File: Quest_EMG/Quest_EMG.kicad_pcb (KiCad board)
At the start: 2 copper layers, 55 x 60 mm, 72 parts, among them IC1 OPA2890IDGST, IC2 OPA2890IDGST, J1 Conn_01x19_Socket, J2 Conn_01x19_Socket, J3 AudioJack3, J4 AudioJack3, J5 Conn_01x10_Pin, U1 AD8620, U2 INA121UAE4, U3 INA121UAE4, U4 L7805

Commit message: cleanup
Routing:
- net GND: vias 104 -> 108
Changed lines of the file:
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@@
       (effects (font (size 0.6 0.6) (thickness 0.15) bold) (justify left top mirror))
     (stroke (width 0.15) (type solid))  )
+  (dimension (type aligned) (layer "User.2")
+    (pts (xy 84.57 79.02) (xy 139.57 79.02))
+    (height 4.011)
+    (gr_text "55.0000 mm" (at 112.07 81.881) (layer "User.2")
+      (effects (font (size 1 1) (thickness 0.15)))
+    )
+    (format (prefix "") (suffix "") (units 3) (units_format 1) (precision 4))
+    (style (thickness 0.15) (arrow_length 1.27) (text_position_mode 0) (extension_height 0.58642) (extension_offset 0.5) keep_text_aligned)
+  )
+  (dimension (type aligned) (layer "User.2")
+    (pts (xy 84.57 79.02) (xy 84.57 19.02))
+    (height -3.385)
+    (gr_text "60.0000 mm" (at 80.035 49.02 90) (layer "User.2")
+      (effects (font (size 1 1) (thickness 0.15)))
+    )
+    (format (prefix "") (suffix "") (units 3) (units_format 1) (precision 4))
+    (style (thickness 0.15) (arrow_length 1.27) (text_position_mode 0) (extension_height 0.58642) (extension_offset 0.5) keep_text_aligned)
+  )
   (segment (start 96.042501 55.297501) (end 96.042501 57.498501) (width 0.25) (layer "F.Cu") (net 1))
   (segment (start 120.767 69.598) (end 121.649 69.598) (width 0.25) (layer "F.Cu") (net 1))
@@
   (via (at 94.831 73.982) (size 0.8) (drill 0.4) (layers "F.Cu" "B.Cu") (free) (net 1))
   (via (at 133.871 65.097) (size 0.8) (drill 0.4) (layers "F.Cu" "B.Cu") (free) (net 1))
+  (via (at 119.486 39.508) (size 0.8) (drill 0.4) (layers "F.Cu" "B.Cu") (free) (net 1))
   (via (at 90.833 71.341) (size 0.8) (drill 0.4) (layers "F.Cu" "B.Cu") (free) (net 1))
   (via (at 130.735 50.407) (size 0.8) (drill 0.4) (layers "F.Cu" "B.Cu") (free) (net 1))
@@
   (via (at 130.68 64.767) (size 0.8) (drill 0.4) (layers "F.Cu" "B.Cu") (free) (net 1))
   (via (at 108.565 26.591) (size 0.8) (drill 0.4) (layers "F.Cu" "B.Cu") (free) (net 1))
+  (via (at 119.405 37.09) (size 0.8) (drill 0.4) (layers "F.Cu" "B.Cu") (free) (net 1))
   (via (at 88.706 71.635) (size 0.8) (drill 0.4) (layers "F.Cu" "B.Cu") (free) (net 1))
   (via (at 114.287 22.088) (size 0.8) (drill 0.4) (layers "F.Cu" "B.Cu") (free) (net 1))
@@
   (via (at 100.48 69.58) (size 0.8) (drill 0.4) (layers "F.Cu" "B.Cu") (free) (net 1))
   (via (at 100.554 72.001) (size 0.8) (drill 0.4) (layers "F.Cu" "B.Cu") (free) (net 1))
+  (via (at 114.649 36.929) (size 0.8) (drill 0.4) (layers "F.Cu" "B.Cu") (free) (net 1))
   (via (at 127.214 68.618) (size 0.8) (drill 0.4) (layers "F.Cu" "B.Cu") (free) (net 1))
   (via (at 122.943 41.923) (size 0.8) (drill 0.4) (layers "F.Cu" "B.Cu") (free) (net 1))
@@
   (via (at 126.248 36.651) (size 0.8) (drill 0.4) (layers "F.Cu" "B.Cu") (free) (net 1))
   (via (at 130.735 55.138) (size 0.8) (drill 0.4) (layers "F.Cu" "B.Cu") (free) (net 1))
+  (via (at 126.337 39.428) (size 0.8) (drill 0.4) (layers "F.Cu" "B.Cu") (free) (net 1))
   (via (at 121.697 30.01) (size 0.8) (drill 0.4) (layers "F.Cu" "B.Cu") (free) (net 1))
   (via (at 93.071 71.671) (size 0.8) (drill 0.4) (layers "F.Cu" "B.Cu") (free) (net 1))
@@
       )
     )
-  )
-  (zone (net 0) (net_name "") (layer "B.Cu") (hatch edge 0.5)
-    (connect_pads (clearance 0))
-    (min_thickness 0.25) (filled_areas_thickness no)
-    (keepout (tracks allowed) (vias allowed) (pads allowed) (copperpour not_allowed) (footprints allowed))
-    (fill (thermal_gap 0.5) (thermal_bridge_width 0.5) (island_removal_mode 1) (island_area_min 10))
-    (polygon
-      (pts
-        (xy 131.6995 34.308)
-        (xy 134.4385 35.949)
-        (xy 134.0365 36.59)
-        (xy 130.3845 36.525)
-        (xy 129.9495 35.829)
-      )
-    )

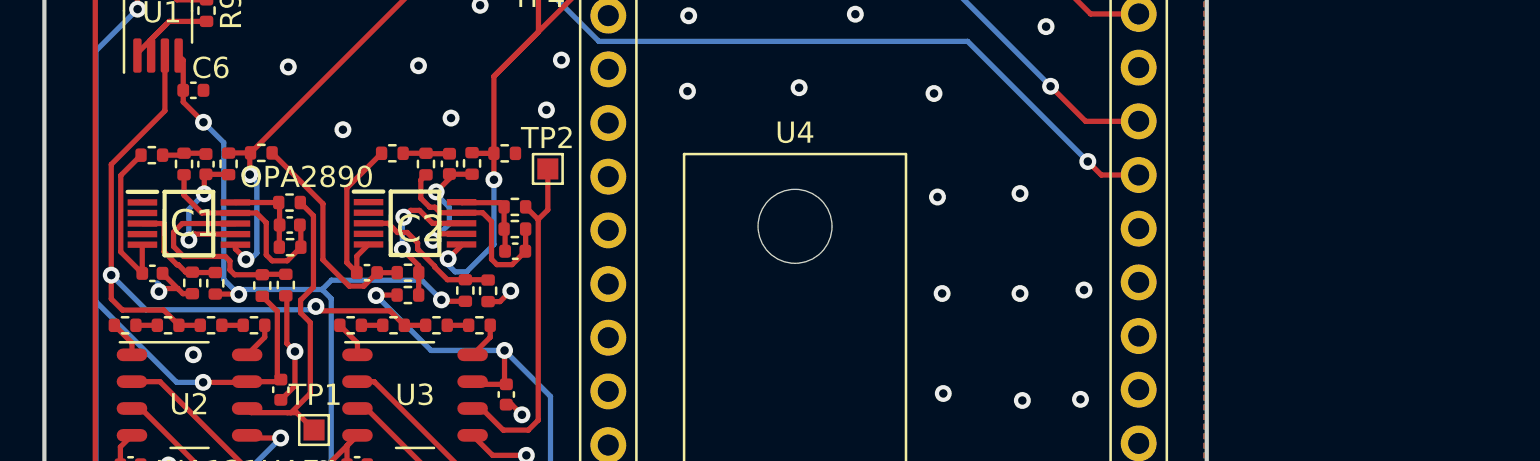
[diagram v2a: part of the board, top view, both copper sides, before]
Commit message: 62 times amplification
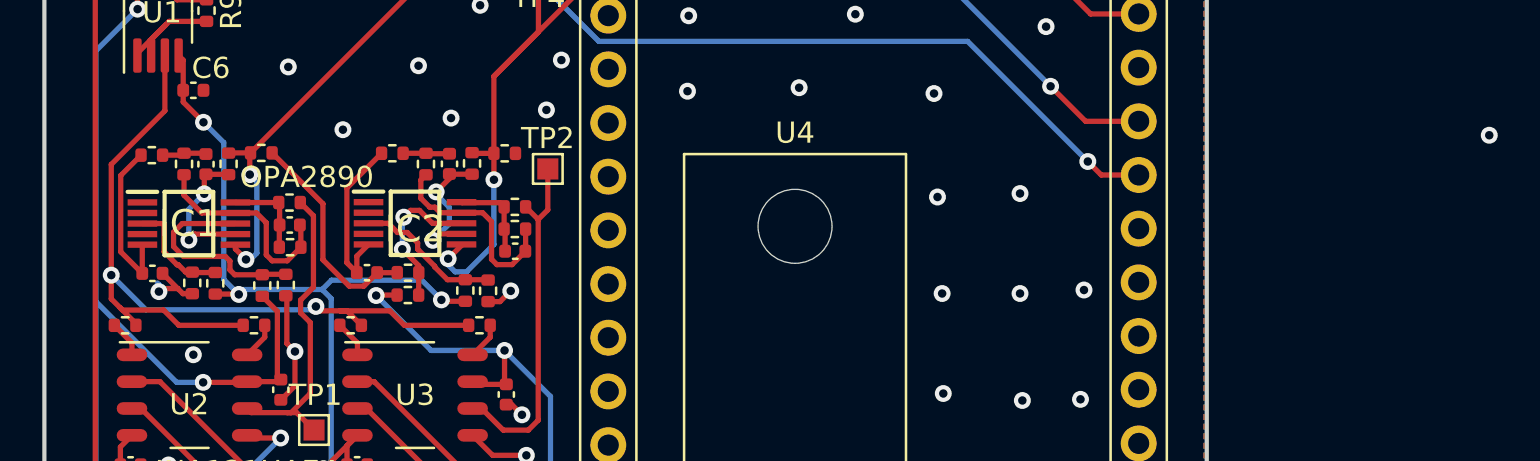
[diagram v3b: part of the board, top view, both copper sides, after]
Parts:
- removed R2, R6: 15, Resistor_SMD:R_0402_1005Metric
- removed R3, R7: 390, Resistor_SMD:R_0402_1005Metric
- R1, R5: value 390 -> 100
- R4, R8: value 15 -> 100
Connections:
- R1 pad 2: Net-(R1-Pad2) -> RL_conn
- R4 pad 1: Net-(R3-Pad2) -> RL_conn
- R5 pad 2: Net-(R5-Pad2) -> RL_conn
- R8 pad 1: Net-(R7-Pad2) -> RL_conn
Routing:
- net RL_conn: track 33.3 -> 39.8 mm
- net Net-(R7-Pad2): track 1.01 -> 0.00 mm
- net Net-(R1-Pad2): track 1.01 -> 0.00 mm
- net Net-(R5-Pad2): track 1.01 -> 0.00 mm
- net Net-(R3-Pad2): track 1.01 -> 0.00 mm
- net (no net): vias 0 -> 1

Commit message: feature amplification
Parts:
- removed C10, C11, C12, C7, C8, C9: 390n, Capacitor_SMD:C_0402_1005Metric
- removed R27, R29: 10k, Resistor_SMD:R_0402_1005Metric
- removed R28: 33k, Resistor_SMD:R_0402_1005Metric
- removed R31: 56k, Resistor_SMD:R_0402_1005Metric
- added R2: 1K, Resistor_SMD:R_0402_1005Metric, F.Cu at (95.6, 50.1)
- added R3: 10K, Resistor_SMD:R_0402_1005Metric, F.Cu at (95.6, 51.1)
- added R6: 1K, Resistor_SMD:R_0402_1005Metric, F.Cu at (96.2, 52.7)
- added R7: 15K, Resistor_SMD:R_0402_1005Metric, F.Cu at (95.1, 52.7)
- R12, R13: value 33k -> 68k
- R14, R15: value 56k -> 15k
- R16, R17: value 10k -> 68k
- R18, R19, R22: value 10k -> 15K
- R20, R23: value 10k -> 1K
- R21: value 10k -> 10K
- R24: value 5k8 -> 56k
- R25: value 5k8 -> 33k
- R26: value 33k -> 56k
- R30: value 56k -> 33k
- moved R20 18.0 mm to (108.7, 52.8), turned to -90 degrees
- moved R24 12.4 mm to (104.4, 54.6)
- moved R22 10.4 mm to (106.6, 52.8), turned to -90 degrees
- moved R19 7.69 mm to (99.1, 51.3), turned to 90 degrees
- moved TP2 7.30 mm to (108.4, 56.5)
- moved R18 6.41 mm to (90.2, 48.4)
- moved R25 5.69 mm to (105.5, 54.6), turned to -90 degrees
- moved R21 5.00 mm to (107.1, 51.3), turned to 0 degrees
- moved R17 4.92 mm to (98.7, 52.8), turned to 0 degrees
- moved R15 3.54 mm to (102.0, 54.6)
- moved R13 3.53 mm to (101.0, 54.6)
- moved R23 1.06 mm to (107.6, 52.8), turned to 90 degrees
- moved R16 0.99 mm to (89.2, 49.5), turned to 0 degrees
- moved IC2 0.76 mm to (102.9, 51.8)
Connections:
- IC1 pad 6: 32 -> Net-(IC1--IN_B)
- IC1 pad 7: Net-(IC1-OUT_B) -> 32
- IC2 pad 6: 33 -> Net-(IC2--IN_B)
- IC2 pad 7: Net-(IC2-OUT_B) -> 33
- R16 pad 1: Net-(C9-Pad2) -> +9V
- R17 pad 1: Net-(C10-Pad2) -> +9V
- R18 pad 1: Net-(IC1--IN_A) -> Net-(IC1-+IN_B)
- R18 pad 2: In_amp1 -> GND
- R19 pad 1: Net-(IC2--IN_A) -> Net-(IC2-+IN_B)
- R19 pad 2: In_amp2 -> GND
- R20 pad 1: Net-(IC1-OUT_A) -> Net-(IC2--IN_A)
- R20 pad 2: Net-(C9-Pad2) -> In_amp2
- R21 pad 2: Net-(C10-Pad2) -> Net-(IC2--IN_A)
- R22 pad 1: Net-(IC1-OUT_A) -> 33
- R22 pad 2: Net-(IC1--IN_A) -> Net-(IC2--IN_B)
- R23 pad 1: Net-(IC2-OUT_A) -> Net-(IC2--IN_B)
- R24 pad 1: Net-(IC1-OUT_B) -> +9V
- R24 pad 2: 32 -> Net-(IC2-+VS)
- R25 pad 1: Net-(IC2-OUT_B) -> Net-(IC2-+VS)
- R25 pad 2: 33 -> GND
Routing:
- net +9V: track 125.5 -> 137.2 mm, vias 5 -> 7
- net Net-(IC1-OUT_A): track 10.0 -> 1.55 mm
- net Net-(IC2-OUT_A): track 9.82 -> 1.55 mm
- net Net-(IC1-OUT_B): track 6.84 -> 0.00 mm, vias 2 -> 0
- net Net-(IC2-OUT_B): track 6.54 -> 0.00 mm, vias 2 -> 0
- net Net-(IC2-+IN_B): track 8.09 -> 2.52 mm
- net In_amp2: track 16.6 -> 12.0 mm
- net -9V: track 70.9 -> 66.9 mm
- net Net-(IC2--IN_B): track 0.00 -> 2.77 mm
- net Net-(IC1--IN_B): track 0.00 -> 2.74 mm
- net GND: track 60.6 -> 63.2 mm, vias 108 -> 111
- net /Bluetooth ESP/3V3: track 27.1 -> 24.5 mm
- net Net-(IC2--VS): track 6.96 -> 4.48 mm
- net Net-(C10-Pad2): track 2.20 -> 0.00 mm
- net Net-(C9-Pad2): track 2.11 -> 0.00 mm
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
